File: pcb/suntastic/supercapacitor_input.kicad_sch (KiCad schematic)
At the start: 0 parts

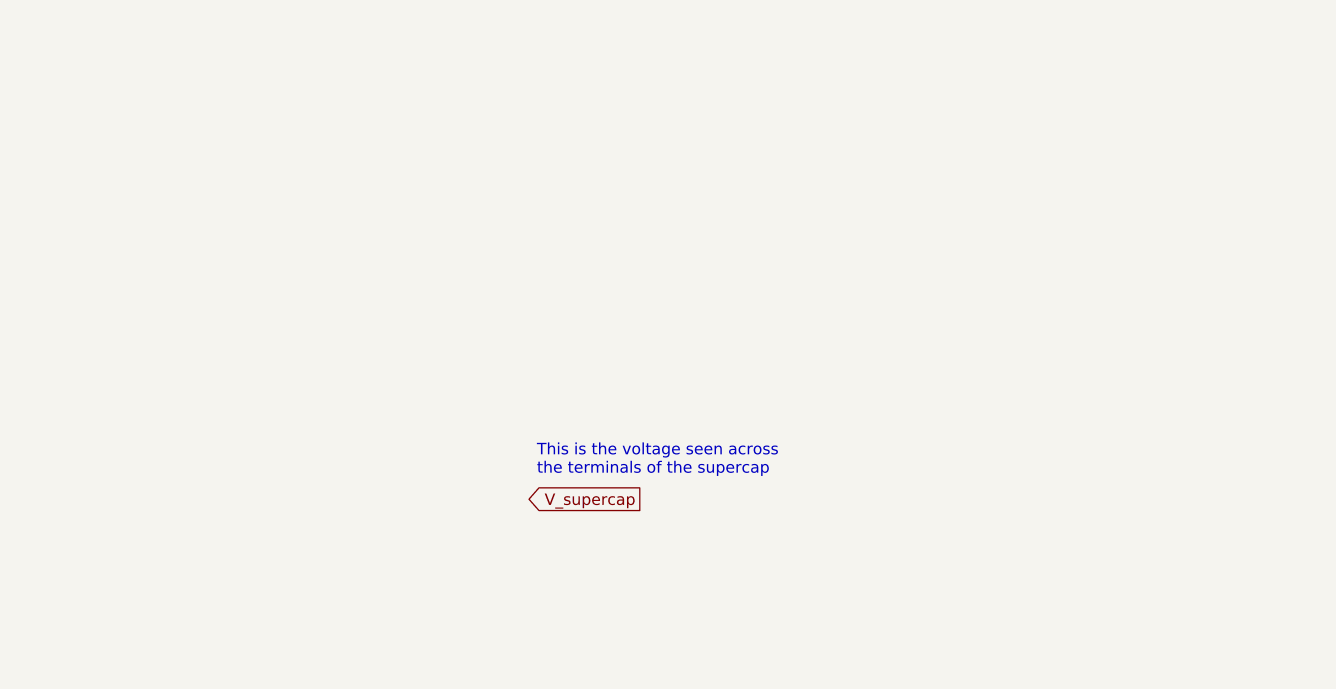
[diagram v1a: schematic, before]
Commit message: Add load switch and RAK connector
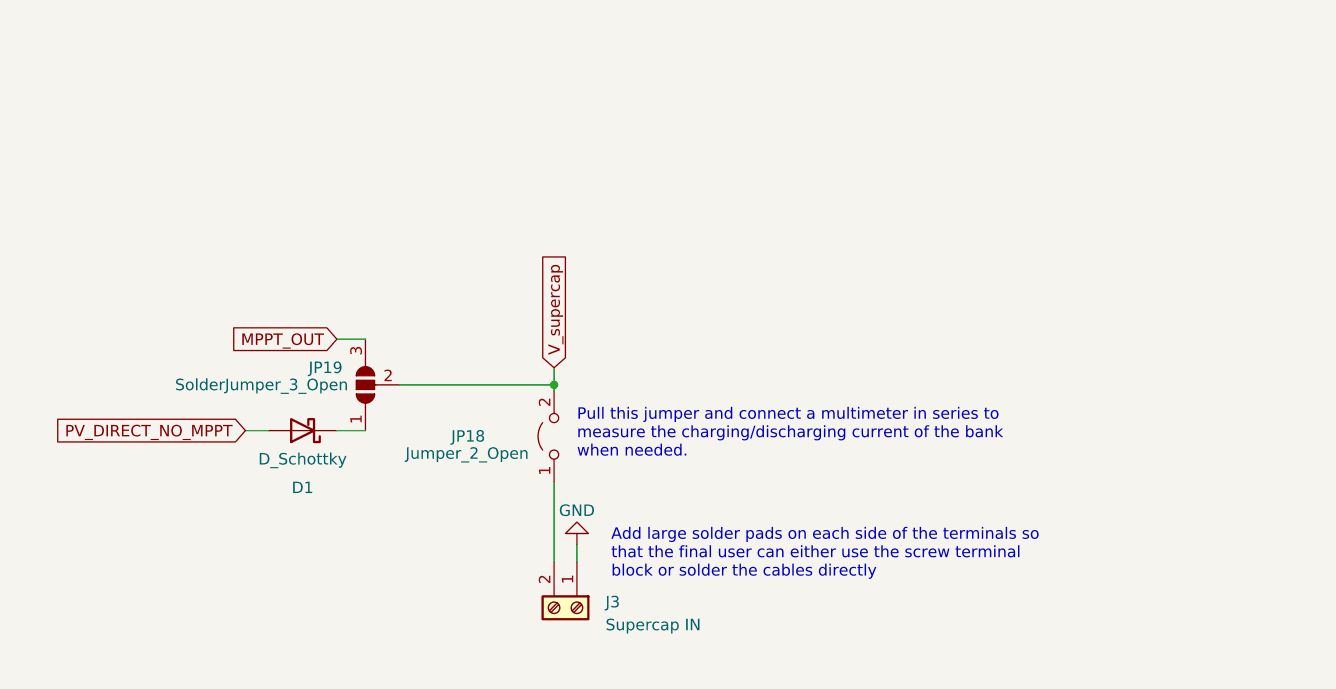
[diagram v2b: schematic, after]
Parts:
- added D1: D_Schottky, symbol Device:D_Schottky
- added J3: Supercap IN, TerminalBlock:TerminalBlock_bornier-2_P5.08mm, symbol Connector:Screw_Terminal_01x02
- added JP18: Jumper_2_Open, symbol Jumper:Jumper_2_Open
- added JP19: SolderJumper_3_Open, symbol Jumper:SolderJumper_3_Open
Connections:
- net V_supercap: now also JP18.2 (B), JP19.2 (C)
- new net: J3.2 (Pin_2), JP18.1 (A)
- new net: D1.1 (K), JP19.1 (A)
- new net GND: J3.1 (Pin_1)
- new net MPPT_OUT: JP19.3 (B)
- new net PV_DIRECT_NO_MPPT: D1.2 (A)
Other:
- note added: "Add large solder pads on each side of the terminals so that the final user can either use the screw terminal block or solder the cables directly"
- note added: "Pull this jumper and connect a multimeter in series to measure the charging/discharging current of the bank when needed."
- note removed: "This is the voltage seen across the terminals of the supercap"
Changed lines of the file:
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@@
     (date "2024-02-07")
     (rev "1")
+    (comment 1 "However, the larger the capacitor, the longer it will take to reach 5.2V.")
+    (comment 2 "The is no limit in the total capacitance of the bank. ")
+    (comment 3 "The MPPT charger can output up to 5.2V and 5W max. ")
+    (comment 4 "The maximum voltage tolerated by the supercapacitor bank should be AT LEAST 5.4V.")
   )
-  (text "This is the voltage seen across\nthe terminals of the supercap"
-    (at 148.59 81.28 0)
+  (junction (at 150.495 71.12) (diameter 0) (color 0 0 0 0)
+  )
+  (wire (pts (xy 150.495 81.915) (xy 150.495 90.805))
+    (stroke (width 0) (type default))
+  )
+  (wire (pts (xy 116.205 76.2) (xy 118.745 76.2))
+    (stroke (width 0) (type default))
+  )
+  (wire (pts (xy 150.495 69.215) (xy 150.495 71.12))
+    (stroke (width 0) (type default))
+  )
+  (wire (pts (xy 150.495 71.12) (xy 150.495 71.755))
+    (stroke (width 0) (type default))
+  )
+  (wire (pts (xy 133.35 71.12) (xy 150.495 71.12))
+    (stroke (width 0) (type default))
+  )
+  (wire (pts (xy 126.365 76.2) (xy 129.54 76.2))
+    (stroke (width 0) (type default))
+  )
+  (wire (pts (xy 153.035 88.9) (xy 153.035 90.805))
+    (stroke (width 0) (type default))
+  )
+  (wire (pts (xy 126.365 66.04) (xy 129.54 66.04))
+    (stroke (width 0) (type default))
+  )
+  (text "Pull this jumper and connect a multimeter in series to\nmeasure the charging/discharging current of the bank\nwhen needed."
+    (at 153.035 79.375 0)
     (effects (font (size 1.27 1.27)) (justify left bottom))
   )
-  (global_label "V_supercap" (shape output) (at 160.02 83.82 180) (fields_autoplaced)
+  (text "Add large solder pads on each side of the terminals so\nthat the final user can either use the screw terminal \nblock or solder the cables directly"
+    (at 156.845 92.71 0)
+    (effects (font (size 1.27 1.27)) (justify left bottom))
+  )
+  (global_label "PV_DIRECT_NO_MPPT" (shape input) (at 116.205 76.2 180) (fields_autoplaced)
     (effects (font (size 1.27 1.27)) (justify right))
-    (property "Intersheetrefs" "${INTERSHEET_REFS}" (at 146.4705 83.82 0)
+    (property "Intersheetrefs" "${INTERSHEET_REFS}" (at 93.8864 76.2 0)
       (effects (font (size 1.27 1.27)) (justify right) hide)
     )
   )
+  (global_label "MPPT_OUT" (shape input) (at 126.365 66.04 180) (fields_autoplaced)
+    (effects (font (size 1.27 1.27)) (justify right))
+    (property "Intersheetrefs" "${INTERSHEET_REFS}" (at 113.904 66.04 0)
+      (effects (font (size 1.27 1.27)) (justify right) hide)
+    )
+  )
+  (global_label "V_supercap" (shape input) (at 150.495 69.215 90) (fields_autoplaced)
+    (effects (font (size 1.27 1.27)) (justify left))
+    (property "Intersheetrefs" "${INTERSHEET_REFS}" (at 150.495 55.6655 90)
+      (effects (font (size 1.27 1.27)) (justify left) hide)
+    )
+  )
+  (symbol (lib_id "Jumper:Jumper_2_Open") (at 150.495 76.835 90) (unit 1)
+    (in_bom yes) (on_board yes) (dnp no)
+    (property "Reference" "JP18" (at 139.065 76.835 90)
+      (effects (font (size 1.27 1.27)) (justify right))
+    )
+    (property "Value" "Jumper_2_Open" (at 133.985 78.74 90)
+      (effects (font (size 1.27 1.27)) (justify right))
+    )
+    (property "Footprint" "" (at 150.495 76.835 0)
+      (effects (font (size 1.27 1.27)) hide)
+    )
+    (property "Datasheet" "~" (at 150.495 76.835 0)
+      (effects (font (size 1.27 1.27)) hide)
+    )
+    (pin "1")
+    (pin "2")
+    (instances
+      (project "suntastic"
+        (path "/4d5a6178-89d6-4824-ac30-5dee40aabff2/70576ca8-d50a-4f6d-b4d0-36474c2d5281"
+          (reference "JP18") (unit 1)
+        )
+      )
+    )
+  )
+  (symbol (lib_id "power:GND") (at 153.035 88.9 180) (unit 1)
+    (in_bom yes) (on_board yes) (dnp no) (fields_autoplaced)
+    (property "Reference" "#PWR026" (at 153.035 82.55 0)
+      (effects (font (size 1.27 1.27)) hide)
+    )
+    (property "Value" "GND" (at 153.035 85.09 0)
+      (effects (font (size 1.27 1.27)))
+    )
+    (property "Footprint" "" (at 153.035 88.9 0)
+      (effects (font (size 1.27 1.27)) hide)
+    )
+    (property "Datasheet" "" (at 153.035 88.9 0)
+      (effects (font (size 1.27 1.27)) hide)
+    )
+    (pin "1")
+    (instances
+      (project "suntastic"
+        (path "/4d5a6178-89d6-4824-ac30-5dee40aabff2/70576ca8-d50a-4f6d-b4d0-36474c2d5281"
+          (reference "#PWR026") (unit 1)
+        )
+      )
+    )
+  )
+  (symbol (lib_id "Device:D_Schottky") (at 122.555 76.2 180) (unit 1)
+    (in_bom yes) (on_board yes) (dnp no)
+    (property "Reference" "D1" (at 122.555 82.55 0)
+      (effects (font (size 1.27 1.27)))
+    )
+    (property "Value" "D_Schottky" (at 122.555 79.375 0)
+      (effects (font (size 1.27 1.27)))
+    )
+    (property "Footprint" "" (at 122.555 76.2 0)
+      (effects (font (size 1.27 1.27)) hide)
+    )
+    (property "Datasheet" "~" (at 122.555 76.2 0)
+      (effects (font (size 1.27 1.27)) hide)
+    )
+    (pin "1")
+    (pin "2")
+    (instances
+      (project "suntastic"
+        (path "/4d5a6178-89d6-4824-ac30-5dee40aabff2/70576ca8-d50a-4f6d-b4d0-36474c2d5281"
+          (reference "D1") (unit 1)
+        )
+      )
+    )
+  )
+  (symbol (lib_id "Connector:Screw_Terminal_01x02") (at 153.035 95.885 270) (unit 1)
+    (in_bom yes) (on_board yes) (dnp no) (fields_autoplaced)
+    (property "Reference" "J3" (at 156.21 95.25 90)
+      (effects (font (size 1.27 1.27)) (justify left))
+    )
+    (property "Value" "Supercap IN" (at 156.21 97.79 90)
+      (effects (font (size 1.27 1.27)) (justify left))
+    )
+    (property "Footprint" "TerminalBlock:TerminalBlock_bornier-2_P5.08mm" (at 153.035 95.885 0)
+      (effects (font (size 1.27 1.27)) hide)
+    )
+    (property "Datasheet" "~" (at 153.035 95.885 0)
+      (effects (font (size 1.27 1.27)) hide)
+    )
+    (pin "1")
+    (pin "2")
+    (instances
+      (project "suntastic"
+        (path "/4d5a6178-89d6-4824-ac30-5dee40aabff2/70576ca8-d50a-4f6d-b4d0-36474c2d5281"
+          (reference "J3") (unit 1)
+        )
+      )
+    )
+  )
+  (symbol (lib_id "Jumper:SolderJumper_3_Open") (at 129.54 71.12 90) (unit 1)
+    (in_bom yes) (on_board yes) (dnp no)
+    (property "Reference" "JP19" (at 127 69.215 90)
+      (effects (font (size 1.27 1.27)) (justify left))
+    )
+    (property "Value" "SolderJumper_3_Open" (at 127.635 71.12 90)
+      (effects (font (size 1.27 1.27)) (justify left))
+    )
+    (property "Footprint" "" (at 129.54 71.12 0)
+      (effects (font (size 1.27 1.27)) hide)
+    )
+    (property "Datasheet" "~" (at 129.54 71.12 0)
+      (effects (font (size 1.27 1.27)) hide)
+    )
+    (pin "1")
+    (pin "2")
+    (pin "3")
+    (instances
+      (project "suntastic"
+        (path "/4d5a6178-89d6-4824-ac30-5dee40aabff2/70576ca8-d50a-4f6d-b4d0-36474c2d5281"
+          (reference "JP19") (unit 1)
+        )
+      )
+    )
+  )

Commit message: Add more doccstrings
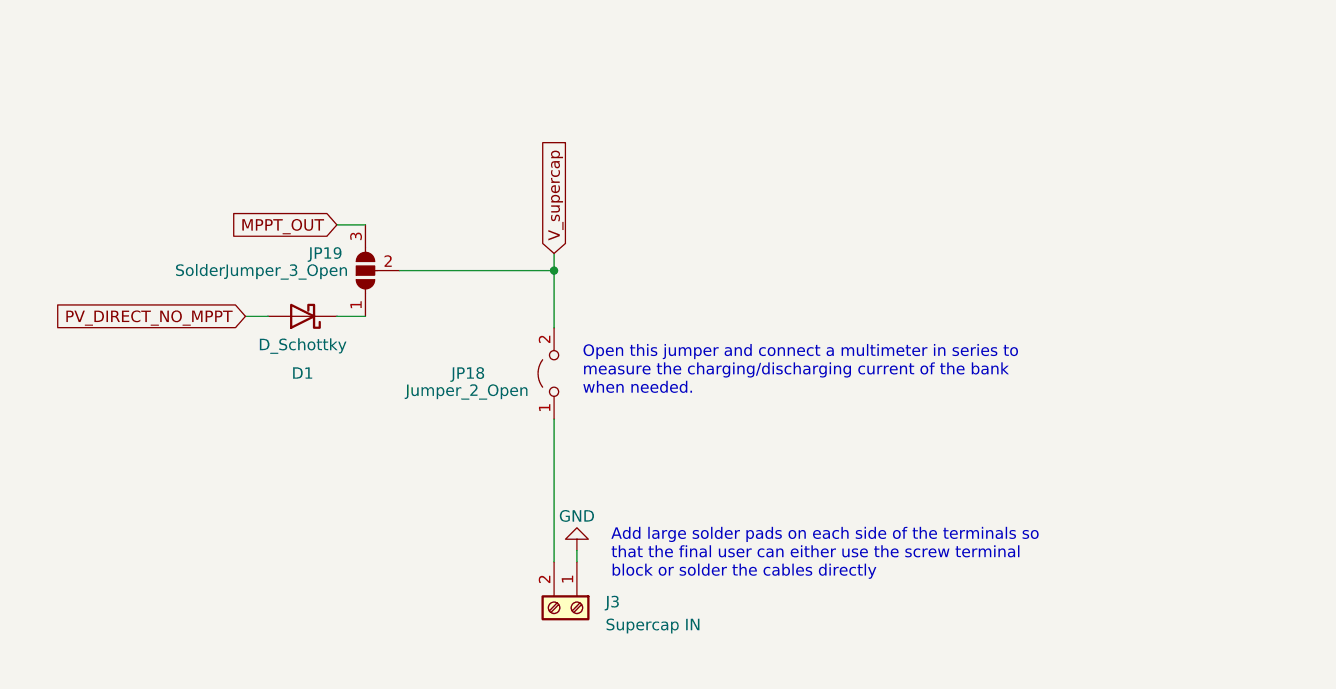
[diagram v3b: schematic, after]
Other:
- note added: "Open this jumper and connect a multimeter in series to measure the charging/discharging current of the bank when needed."
- note removed: "Pull this jumper and connect a multimeter in series to measure the charging/discharging current of the bank when needed."
- moved on the sheet: D1, JP18, JP19
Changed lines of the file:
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@@
     (comment 1 "However, the larger the capacitor, the longer it will take to reach 5.2V.")
     (comment 2 "The is no limit in the total capacitance of the bank. ")
-    (comment 3 "The MPPT charger can output up to 5.2V and 5W max. ")
+    (comment 3 "The MPPT charger based on the SPV1040 can output up to 5.2V and 5W max. ")
     (comment 4 "The maximum voltage tolerated by the supercapacitor bank should be AT LEAST 5.4V.")
   )
-  (junction (at 150.495 71.12) (diameter 0) (color 0 0 0 0)
+  (junction (at 150.495 58.42) (diameter 0) (color 0 0 0 0)
   )
-  (wire (pts (xy 150.495 81.915) (xy 150.495 90.805))
+  (wire (pts (xy 150.495 74.93) (xy 150.495 90.805))
     (stroke (width 0) (type default))
   )
-  (wire (pts (xy 116.205 76.2) (xy 118.745 76.2))
+  (wire (pts (xy 116.205 63.5) (xy 118.745 63.5))
     (stroke (width 0) (type default))
   )
-  (wire (pts (xy 150.495 69.215) (xy 150.495 71.12))
+  (wire (pts (xy 150.495 56.515) (xy 150.495 58.42))
     (stroke (width 0) (type default))
   )
-  (wire (pts (xy 150.495 71.12) (xy 150.495 71.755))
+  (wire (pts (xy 150.495 58.42) (xy 150.495 64.77))
     (stroke (width 0) (type default))
   )
-  (wire (pts (xy 133.35 71.12) (xy 150.495 71.12))
+  (wire (pts (xy 133.35 58.42) (xy 150.495 58.42))
     (stroke (width 0) (type default))
   )
-  (wire (pts (xy 126.365 76.2) (xy 129.54 76.2))
+  (wire (pts (xy 126.365 63.5) (xy 129.54 63.5))
     (stroke (width 0) (type default))
   )
-  (wire (pts (xy 153.035 88.9) (xy 153.035 90.805))
+  (wire (pts (xy 153.035 89.535) (xy 153.035 90.805))
     (stroke (width 0) (type default))
   )
-  (wire (pts (xy 126.365 66.04) (xy 129.54 66.04))
+  (wire (pts (xy 126.365 53.34) (xy 129.54 53.34))
     (stroke (width 0) (type default))
   )
-  (text "Pull this jumper and connect a multimeter in series to\nmeasure the charging/discharging current of the bank\nwhen needed."
-    (at 153.035 79.375 0)
+  (text "Open this jumper and connect a multimeter in series to\nmeasure the charging/discharging current of the bank\nwhen needed."
+    (at 153.67 72.39 0)
     (effects (font (size 1.27 1.27)) (justify left bottom))
   )
@@
     (effects (font (size 1.27 1.27)) (justify left bottom))
   )
-  (global_label "PV_DIRECT_NO_MPPT" (shape input) (at 116.205 76.2 180) (fields_autoplaced)
+  (global_label "PV_DIRECT_NO_MPPT" (shape input) (at 116.205 63.5 180) (fields_autoplaced)
     (effects (font (size 1.27 1.27)) (justify right))
-    (property "Intersheetrefs" "${INTERSHEET_REFS}" (at 93.8864 76.2 0)
+    (property "Intersheetrefs" "${INTERSHEET_REFS}" (at 93.8864 63.5 0)
       (effects (font (size 1.27 1.27)) (justify right) hide)
     )
   )
-  (global_label "MPPT_OUT" (shape input) (at 126.365 66.04 180) (fields_autoplaced)
+  (global_label "MPPT_OUT" (shape input) (at 126.365 53.34 180) (fields_autoplaced)
     (effects (font (size 1.27 1.27)) (justify right))
-    (property "Intersheetrefs" "${INTERSHEET_REFS}" (at 113.904 66.04 0)
+    (property "Intersheetrefs" "${INTERSHEET_REFS}" (at 113.904 53.34 0)
       (effects (font (size 1.27 1.27)) (justify right) hide)
     )
   )
-  (global_label "V_supercap" (shape input) (at 150.495 69.215 90) (fields_autoplaced)
+  (global_label "V_supercap" (shape input) (at 150.495 56.515 90) (fields_autoplaced)
     (effects (font (size 1.27 1.27)) (justify left))
-    (property "Intersheetrefs" "${INTERSHEET_REFS}" (at 150.495 55.6655 90)
+    (property "Intersheetrefs" "${INTERSHEET_REFS}" (at 150.495 42.9655 90)
       (effects (font (size 1.27 1.27)) (justify left) hide)
     )
   )
-  (symbol (lib_id "Jumper:Jumper_2_Open") (at 150.495 76.835 90) (unit 1)
+  (symbol (lib_id "Jumper:Jumper_2_Open") (at 150.495 69.85 90) (unit 1)
     (in_bom yes) (on_board yes) (dnp no)
-    (property "Reference" "JP18" (at 139.065 76.835 90)
+    (property "Reference" "JP18" (at 139.065 69.85 90)
       (effects (font (size 1.27 1.27)) (justify right))
     )
-    (property "Value" "Jumper_2_Open" (at 133.985 78.74 90)
+    (property "Value" "Jumper_2_Open" (at 133.985 71.755 90)
       (effects (font (size 1.27 1.27)) (justify right))
     )
-    (property "Footprint" "" (at 150.495 76.835 0)
+    (property "Footprint" "" (at 150.495 69.85 0)
       (effects (font (size 1.27 1.27)) hide)
     )
-    (property "Datasheet" "~" (at 150.495 76.835 0)
+    (property "Datasheet" "~" (at 150.495 69.85 0)
       (effects (font (size 1.27 1.27)) hide)
     )
@@
     )
   )
-  (symbol (lib_id "power:GND") (at 153.035 88.9 180) (unit 1)
+  (symbol (lib_id "power:GND") (at 153.035 89.535 180) (unit 1)
     (in_bom yes) (on_board yes) (dnp no) (fields_autoplaced)
-    (property "Reference" "#PWR026" (at 153.035 82.55 0)
+    (property "Reference" "#PWR026" (at 153.035 83.185 0)
       (effects (font (size 1.27 1.27)) hide)
     )
-    (property "Value" "GND" (at 153.035 85.09 0)
+    (property "Value" "GND" (at 153.035 85.725 0)
       (effects (font (size 1.27 1.27)))
     )
-    (property "Footprint" "" (at 153.035 88.9 0)
+    (property "Footprint" "" (at 153.035 89.535 0)
       (effects (font (size 1.27 1.27)) hide)
     )
-    (property "Datasheet" "" (at 153.035 88.9 0)
+    (property "Datasheet" "" (at 153.035 89.535 0)
       (effects (font (size 1.27 1.27)) hide)
     )
@@
     )
   )
-  (symbol (lib_id "Device:D_Schottky") (at 122.555 76.2 180) (unit 1)
+  (symbol (lib_id "Device:D_Schottky") (at 122.555 63.5 180) (unit 1)
     (in_bom yes) (on_board yes) (dnp no)
-    (property "Reference" "D1" (at 122.555 82.55 0)
+    (property "Reference" "D1" (at 122.555 69.85 0)
       (effects (font (size 1.27 1.27)))
     )
-    (property "Value" "D_Schottky" (at 122.555 79.375 0)
+    (property "Value" "D_Schottky" (at 122.555 66.675 0)
       (effects (font (size 1.27 1.27)))
     )
-    (property "Footprint" "" (at 122.555 76.2 0)
+    (property "Footprint" "" (at 122.555 63.5 0)
       (effects (font (size 1.27 1.27)) hide)
     )
-    (property "Datasheet" "~" (at 122.555 76.2 0)
+    (property "Datasheet" "~" (at 122.555 63.5 0)
       (effects (font (size 1.27 1.27)) hide)
     )
@@
     )
   )
-  (symbol (lib_id "Jumper:SolderJumper_3_Open") (at 129.54 71.12 90) (unit 1)
+  (symbol (lib_id "Jumper:SolderJumper_3_Open") (at 129.54 58.42 90) (unit 1)
     (in_bom yes) (on_board yes) (dnp no)
-    (property "Reference" "JP19" (at 127 69.215 90)
+    (property "Reference" "JP19" (at 127 56.515 90)
       (effects (font (size 1.27 1.27)) (justify left))
     )
-    (property "Value" "SolderJumper_3_Open" (at 127.635 71.12 90)
+    (property "Value" "SolderJumper_3_Open" (at 127.635 58.42 90)
       (effects (font (size 1.27 1.27)) (justify left))
     )
-    (property "Footprint" "" (at 129.54 71.12 0)
+    (property "Footprint" "" (at 129.54 58.42 0)
       (effects (font (size 1.27 1.27)) hide)
     )
-    (property "Datasheet" "~" (at 129.54 71.12 0)
+    (property "Datasheet" "~" (at 129.54 58.42 0)
       (effects (font (size 1.27 1.27)) hide)
     )
